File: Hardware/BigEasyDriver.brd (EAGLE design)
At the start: 36.8 x 30.5 mm, 53 parts, among them IC1 A4983ALT1, IC2 LM317L

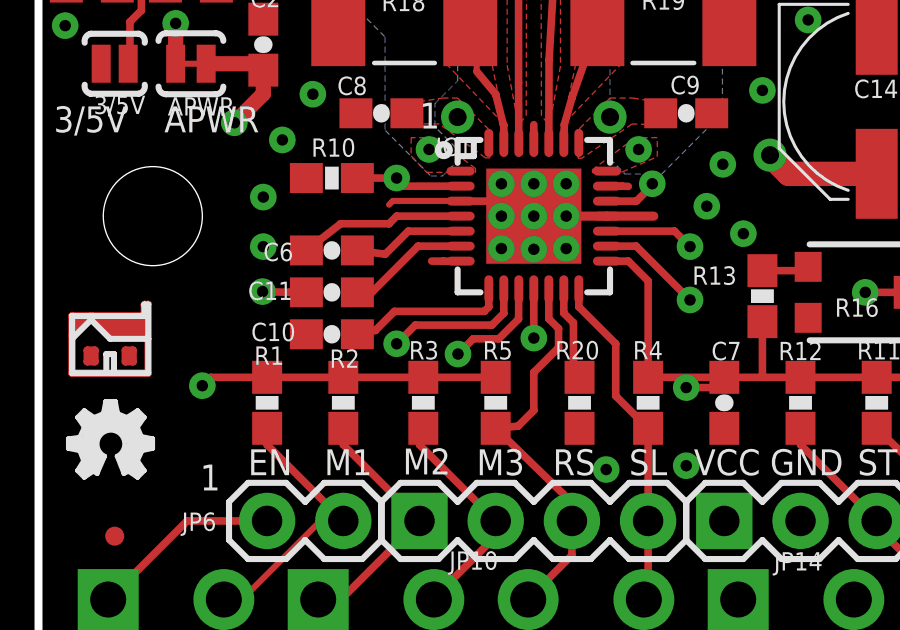
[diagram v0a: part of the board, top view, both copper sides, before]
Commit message: Changed Schematic Nets
Nets changed to new specifications
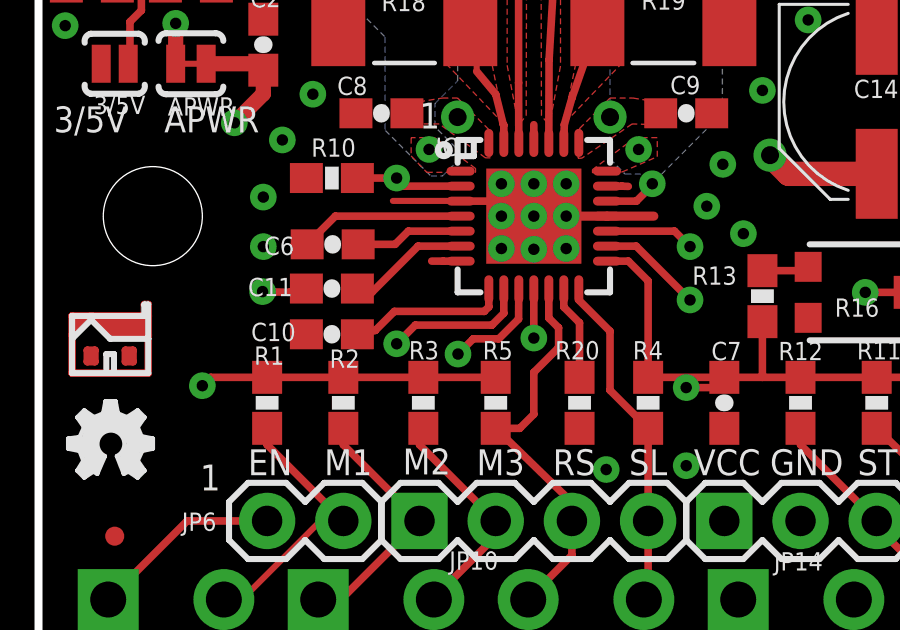
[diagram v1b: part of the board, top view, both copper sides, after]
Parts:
- moved C6 0.20 mm to (9.80, 14.3)
- moved C11 0.13 mm to (9.78, 12.8)
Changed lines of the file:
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@@
 <setting verticaltext="up"/>
 </settings>
-<grid distance="0.05" unitdist="inch" unit="inch" style="lines" multiple="1" display="yes" altdistance="0.005" altunitdist="inch" altunit="inch"/>
+<grid distance="0.05" unitdist="inch" unit="inch" style="lines" multiple="1" display="yes" altdistance="0.001" altunitdist="inch" altunit="inch"/>
 <layers>
 <layer number="1" name="Top" color="4" fill="1" visible="yes" active="yes"/>
@@
 <layer number="27" name="tValues" color="7" fill="1" visible="no" active="yes"/>
 <layer number="28" name="bValues" color="7" fill="1" visible="no" active="yes"/>
-<layer number="29" name="tStop" color="7" fill="3" visible="yes" active="yes"/>
+<layer number="29" name="tStop" color="7" fill="3" visible="no" active="yes"/>
 <layer number="30" name="bStop" color="7" fill="6" visible="no" active="yes"/>
 <layer number="31" name="tCream" color="7" fill="4" visible="no" active="yes"/>
@@
 <layer number="13" name="Route13" color="4" fill="5" visible="no" active="no"/>
 <layer number="14" name="Route14" color="1" fill="6" visible="no" active="no"/>
-<layer number="15" name="GND" color="13" fill="1" visible="yes" active="yes"/>
-<layer number="2" name="VCC" color="14" fill="1" visible="yes" active="yes"/>
+<layer number="15" name="GND" color="13" fill="1" visible="no" active="yes"/>
+<layer number="2" name="VCC" color="14" fill="1" visible="no" active="yes"/>
 <layer number="3" name="Route3" color="4" fill="3" visible="no" active="no"/>
 <layer number="4" name="Route4" color="1" fill="4" visible="no" active="no"/>
@@
 </class>
 </classes>
-<designrules name="SparkFun *">
+<designrules name="SparkFun">
 <description language="en">&lt;b&gt;EAGLE Design Rules&lt;/b&gt;
 &lt;p&gt;
@@
 <param name="mlMinCreamFrame" value="0mil"/>
 <param name="mlMaxCreamFrame" value="0mil"/>
-<param name="mlViaStopLimit" value="24mil"/>
+<param name="mlViaStopLimit" value="20mil"/>
 <param name="srRoundness" value="0"/>
 <param name="srMinRoundness" value="0mil"/>
@@
 <attribute name="VALUE" x="17.2466" y="6.8834" size="0.6096" layer="27"/>
 </element>
-<element name="C6" library="SparkFun" package="0603-CAP" value=".1uf" x="9.779" y="14.097" smashed="yes">
-<attribute name="NAME" x="7.493" y="13.7414" size="0.6096" layer="25" font="vector"/>
-<attribute name="VALUE" x="11.0236" y="13.8684" size="0.6096" layer="27" font="vector"/>
+<element name="C6" library="SparkFun" package="0603-CAP" value=".1uf" x="9.8044" y="14.3002" smashed="yes">
+<attribute name="NAME" x="7.5184" y="13.9446" size="0.6096" layer="25" font="vector"/>
+<attribute name="VALUE" x="11.049" y="14.0716" size="0.6096" layer="27" font="vector"/>
 </element>
 <element name="C7" library="SparkFun" package="0603-CAP" value=".1uf" x="22.86" y="9.017" smashed="yes" rot="R270">
@@
 <attribute name="VALUE" x="11.0236" y="11.0744" size="0.6096" layer="27" font="vector"/>
 </element>
-<element name="C11" library="SparkFun" package="0603-CAP" value=".1uf" x="9.779" y="12.7" smashed="yes" rot="R180">
-<attribute name="NAME" x="6.985" y="12.446" size="0.6096" layer="25" font="vector"/>
-<attribute name="VALUE" x="10.9728" y="12.446" size="0.6096" layer="27" font="vector"/>
+<element name="C11" library="SparkFun" package="0603-CAP" value=".1uf" x="9.779" y="12.827" smashed="yes" rot="R180">
+<attribute name="NAME" x="6.985" y="12.573" size="0.6096" layer="25" font="vector"/>
+<attribute name="VALUE" x="10.9728" y="12.573" size="0.6096" layer="27" font="vector"/>
 </element>
 <element name="D1" library="diode" package="DO-214AC" value="B340A-13-F" x="33.02" y="25.4" smashed="yes" rot="R90">
@@
 <wire x1="15.3035" y1="15.367" x2="15.4305" y2="15.24" width="0.254" layer="1"/>
 <wire x1="11.811" y1="15.748" x2="15.3035" y2="15.748" width="0.2032" layer="1"/>
-<wire x1="11.684" y1="15.621" x2="11.811" y2="15.748" width="0.2032" layer="1"/>
 <via x="15.4305" y="16.3195" extent="1-16" drill="0.381"/>
 <via x="16.51" y="16.3195" extent="1-16" drill="0.381"/>
@@
 <wire x1="9.271" y1="28.702" x2="8.763" y2="29.21" width="0.4064" layer="2"/>
 <wire x1="13.97" y1="18.542" x2="9.271" y2="23.241" width="0.4064" layer="2"/>
-<wire x1="8.929" y1="12.7" x2="8.3566" y2="12.7" width="0.254" layer="1"/>
+<wire x1="8.929" y1="12.827" x2="8.3566" y2="12.7" width="0.254" layer="1"/>
 <wire x1="8.3566" y1="12.7" x2="7.4676" y2="12.7254" width="0.254" layer="1"/>
 <wire x1="8.5344" y1="16.4084" x2="10.668" y2="18.542" width="0.254" layer="2"/>
@@
 <wire x1="16.3222" y1="2.4792" x2="17.78" y2="3.937" width="0.254" layer="1"/>
 <wire x1="17.78" y1="3.937" x2="17.78" y2="5.08" width="0.254" layer="1"/>
-<wire x1="17.01" y1="11.819" x2="17.01" y2="12.8" width="0.254" layer="1"/>
-<wire x1="17.3355" y1="11.4935" x2="17.01" y2="11.819" width="0.254" layer="1"/>
-<wire x1="17.3355" y1="10.8585" x2="17.3355" y2="11.4935" width="0.254" layer="1"/>
+<wire x1="17.01" y1="11.8444" x2="17.01" y2="12.8" width="0.254" layer="1"/>
+<wire x1="17.3355" y1="11.5189" x2="17.01" y2="11.8444" width="0.254" layer="1"/>
+<wire x1="17.3355" y1="10.8585" x2="17.3355" y2="11.5189" width="0.254" layer="1"/>
 <wire x1="16.51" y1="10.033" x2="17.3355" y2="10.8585" width="0.254" layer="1"/>
-<wire x1="16.51" y1="8.763" x2="16.51" y2="10.033" width="0.254" layer="1"/>
-<wire x1="15.987" y1="8.24" x2="16.51" y2="8.763" width="0.254" layer="1"/>
-<wire x1="15.24" y1="8.167" x2="15.987" y2="8.24" width="0.254" layer="1"/>
 <wire x1="17.78" y1="5.08" x2="17.78" y2="5.7" width="0.254" layer="1"/>
 <wire x1="17.78" y1="5.7" x2="15.24" y2="8.167" width="0.254" layer="1"/>
+<wire x1="16.51" y1="10.033" x2="16.51" y2="8.636" width="0.254" layer="1"/>
+<wire x1="16.51" y1="8.636" x2="16.041" y2="8.167" width="0.254" layer="1"/>
+<wire x1="16.041" y1="8.167" x2="15.24" y2="8.167" width="0.254" layer="1"/>
 </signal>
 <signal name="STEP">
@@
 <wire x1="20.1778" y1="2.46" x2="20.32" y2="2.6022" width="0.254" layer="1"/>
 <wire x1="20.32" y1="5.08" x2="20.32" y2="8.167" width="0.254" layer="1"/>
-<wire x1="18.01" y1="12.216" x2="18.01" y2="12.8001" width="0.254" layer="1"/>
-<wire x1="19.2405" y1="10.9855" x2="18.01" y2="12.216" width="0.254" layer="1"/>
-<wire x1="19.2405" y1="10.9855" x2="19.2405" y2="9.2465" width="0.254" layer="1"/>
-<wire x1="19.2405" y1="9.2465" x2="20.32" y2="8.167" width="0.254" layer="1"/>
+<wire x1="18.01" y1="12.8001" x2="18.01" y2="12.4446" width="0.254" layer="1"/>
+<wire x1="18.01" y1="12.4446" x2="19.05" y2="11.4046" width="0.254" layer="1"/>
+<wire x1="19.05" y1="11.4046" x2="19.05" y2="9.437" width="0.254" layer="1"/>
+<wire x1="19.05" y1="9.437" x2="20.32" y2="8.167" width="0.254" layer="1"/>
 </signal>
 <signal name="5V_ALT">
@@
 <contactref element="IC1" pad="P$4"/>
 <contactref element="C6" pad="1"/>
-<wire x1="11.938" y1="15.24" x2="14.0701" y2="15.24" width="0.254" layer="1"/>
-<wire x1="11.938" y1="15.24" x2="11.684" y2="14.986" width="0.254" layer="1"/>
-<wire x1="11.684" y1="14.986" x2="10.072" y2="14.986" width="0.254" layer="1"/>
-<wire x1="10.072" y1="14.986" x2="8.929" y2="14.097" width="0.254" layer="1"/>
+<wire x1="14.0701" y1="15.24" x2="9.8942" y2="15.24" width="0.254" layer="1"/>
+<wire x1="9.8942" y1="15.24" x2="8.9544" y2="14.3002" width="0.254" layer="1"/>
 </signal>
 <signal name="N$9">
@@
 <contactref element="C6" pad="2"/>
 <wire x1="12.327" y1="14.74" x2="14.0702" y2="14.74" width="0.254" layer="1"/>
-<wire x1="11.557" y1="13.97" x2="12.327" y2="14.74" width="0.254" layer="1"/>
-<wire x1="10.629" y1="14.097" x2="11.557" y2="13.97" width="0.254" layer="1"/>
+<wire x1="12.327" y1="14.74" x2="11.8872" y2="14.3002" width="0.254" layer="1"/>
+<wire x1="11.8872" y1="14.3002" x2="10.6544" y2="14.3002" width="0.254" layer="1"/>
 </signal>
 <signal name="N$19">
@@
 <contactref element="R20" pad="1"/>
 <wire x1="17.7546" y1="9.5654" x2="18.034" y2="9.867" width="0.254" layer="1"/>
-<wire x1="17.51" y1="12.0048" x2="17.51" y2="12.8001" width="0.254" layer="1"/>
-<wire x1="17.8308" y1="11.684" x2="17.51" y2="12.0048" width="0.254" layer="1"/>
-<wire x1="17.8308" y1="9.5908" x2="17.8308" y2="11.684" width="0.254" layer="1"/>
 <wire x1="18.034" y1="9.867" x2="17.8308" y2="9.5908" width="0.254" layer="1"/>
+<wire x1="18.1102" y1="9.9432" x2="18.034" y2="9.867" width="0.254" layer="1"/>
+<wire x1="17.51" y1="12.8001" x2="17.51" y2="12.208" width="0.254" layer="1"/>
+<wire x1="17.51" y1="12.208" x2="18.034" y2="11.684" width="0.254" layer="1"/>
+<wire x1="18.034" y1="11.684" x2="18.034" y2="9.867" width="0.254" layer="1"/>
 </signal>
 <signal name="N$20">
@@
 <wire x1="12.6525" y1="14.24" x2="14.0702" y2="14.24" width="0.254" layer="1"/>
 <wire x1="11.1125" y1="12.7" x2="12.6525" y2="14.24" width="0.254" layer="1"/>
-<wire x1="10.629" y1="12.7" x2="11.1125" y2="12.7" width="0.254" layer="1"/>
+<wire x1="10.629" y1="12.827" x2="11.1125" y2="12.7" width="0.254" layer="1"/>
 </signal>
 <signal name="MS3">

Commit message: Revert "Changed Schematic Nets"
This reverts commit ceb7b9bd87dc9e1a8942882cf4505f035ac33b39.
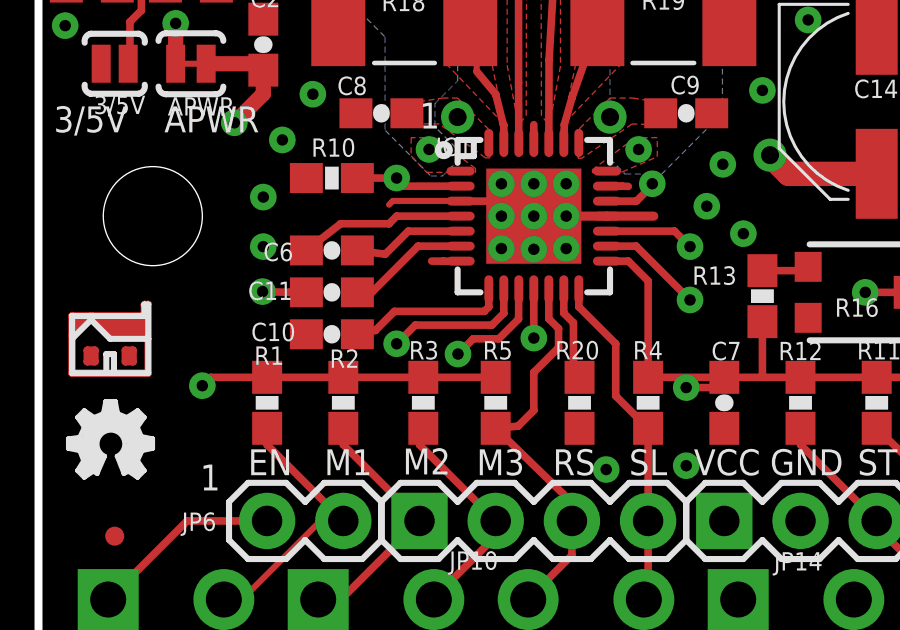
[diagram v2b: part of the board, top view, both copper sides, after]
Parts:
- moved C6 0.20 mm to (9.78, 14.1)
- moved C11 0.13 mm to (9.78, 12.7)
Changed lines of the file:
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@@
 <setting verticaltext="up"/>
 </settings>
-<grid distance="0.05" unitdist="inch" unit="inch" style="lines" multiple="1" display="yes" altdistance="0.001" altunitdist="inch" altunit="inch"/>
+<grid distance="0.05" unitdist="inch" unit="inch" style="lines" multiple="1" display="yes" altdistance="0.005" altunitdist="inch" altunit="inch"/>
 <layers>
 <layer number="1" name="Top" color="4" fill="1" visible="yes" active="yes"/>
@@
 <layer number="27" name="tValues" color="7" fill="1" visible="no" active="yes"/>
 <layer number="28" name="bValues" color="7" fill="1" visible="no" active="yes"/>
-<layer number="29" name="tStop" color="7" fill="3" visible="no" active="yes"/>
+<layer number="29" name="tStop" color="7" fill="3" visible="yes" active="yes"/>
 <layer number="30" name="bStop" color="7" fill="6" visible="no" active="yes"/>
 <layer number="31" name="tCream" color="7" fill="4" visible="no" active="yes"/>
@@
 <layer number="13" name="Route13" color="4" fill="5" visible="no" active="no"/>
 <layer number="14" name="Route14" color="1" fill="6" visible="no" active="no"/>
-<layer number="15" name="GND" color="13" fill="1" visible="no" active="yes"/>
-<layer number="2" name="VCC" color="14" fill="1" visible="no" active="yes"/>
+<layer number="15" name="GND" color="13" fill="1" visible="yes" active="yes"/>
+<layer number="2" name="VCC" color="14" fill="1" visible="yes" active="yes"/>
 <layer number="3" name="Route3" color="4" fill="3" visible="no" active="no"/>
 <layer number="4" name="Route4" color="1" fill="4" visible="no" active="no"/>
@@
 </class>
 </classes>
-<designrules name="SparkFun">
+<designrules name="SparkFun *">
 <description language="en">&lt;b&gt;EAGLE Design Rules&lt;/b&gt;
 &lt;p&gt;
@@
 <param name="mlMinCreamFrame" value="0mil"/>
 <param name="mlMaxCreamFrame" value="0mil"/>
-<param name="mlViaStopLimit" value="20mil"/>
+<param name="mlViaStopLimit" value="24mil"/>
 <param name="srRoundness" value="0"/>
 <param name="srMinRoundness" value="0mil"/>
@@
 <attribute name="VALUE" x="17.2466" y="6.8834" size="0.6096" layer="27"/>
 </element>
-<element name="C6" library="SparkFun" package="0603-CAP" value=".1uf" x="9.8044" y="14.3002" smashed="yes">
-<attribute name="NAME" x="7.5184" y="13.9446" size="0.6096" layer="25" font="vector"/>
-<attribute name="VALUE" x="11.049" y="14.0716" size="0.6096" layer="27" font="vector"/>
+<element name="C6" library="SparkFun" package="0603-CAP" value=".1uf" x="9.779" y="14.097" smashed="yes">
+<attribute name="NAME" x="7.493" y="13.7414" size="0.6096" layer="25" font="vector"/>
+<attribute name="VALUE" x="11.0236" y="13.8684" size="0.6096" layer="27" font="vector"/>
 </element>
 <element name="C7" library="SparkFun" package="0603-CAP" value=".1uf" x="22.86" y="9.017" smashed="yes" rot="R270">
@@
 <attribute name="VALUE" x="11.0236" y="11.0744" size="0.6096" layer="27" font="vector"/>
 </element>
-<element name="C11" library="SparkFun" package="0603-CAP" value=".1uf" x="9.779" y="12.827" smashed="yes" rot="R180">
-<attribute name="NAME" x="6.985" y="12.573" size="0.6096" layer="25" font="vector"/>
-<attribute name="VALUE" x="10.9728" y="12.573" size="0.6096" layer="27" font="vector"/>
+<element name="C11" library="SparkFun" package="0603-CAP" value=".1uf" x="9.779" y="12.7" smashed="yes" rot="R180">
+<attribute name="NAME" x="6.985" y="12.446" size="0.6096" layer="25" font="vector"/>
+<attribute name="VALUE" x="10.9728" y="12.446" size="0.6096" layer="27" font="vector"/>
 </element>
 <element name="D1" library="diode" package="DO-214AC" value="B340A-13-F" x="33.02" y="25.4" smashed="yes" rot="R90">
@@
 <wire x1="15.3035" y1="15.367" x2="15.4305" y2="15.24" width="0.254" layer="1"/>
 <wire x1="11.811" y1="15.748" x2="15.3035" y2="15.748" width="0.2032" layer="1"/>
+<wire x1="11.684" y1="15.621" x2="11.811" y2="15.748" width="0.2032" layer="1"/>
 <via x="15.4305" y="16.3195" extent="1-16" drill="0.381"/>
 <via x="16.51" y="16.3195" extent="1-16" drill="0.381"/>
@@
 <wire x1="9.271" y1="28.702" x2="8.763" y2="29.21" width="0.4064" layer="2"/>
 <wire x1="13.97" y1="18.542" x2="9.271" y2="23.241" width="0.4064" layer="2"/>
-<wire x1="8.929" y1="12.827" x2="8.3566" y2="12.7" width="0.254" layer="1"/>
+<wire x1="8.929" y1="12.7" x2="8.3566" y2="12.7" width="0.254" layer="1"/>
 <wire x1="8.3566" y1="12.7" x2="7.4676" y2="12.7254" width="0.254" layer="1"/>
 <wire x1="8.5344" y1="16.4084" x2="10.668" y2="18.542" width="0.254" layer="2"/>
@@
 <wire x1="16.3222" y1="2.4792" x2="17.78" y2="3.937" width="0.254" layer="1"/>
 <wire x1="17.78" y1="3.937" x2="17.78" y2="5.08" width="0.254" layer="1"/>
-<wire x1="17.01" y1="11.8444" x2="17.01" y2="12.8" width="0.254" layer="1"/>
-<wire x1="17.3355" y1="11.5189" x2="17.01" y2="11.8444" width="0.254" layer="1"/>
-<wire x1="17.3355" y1="10.8585" x2="17.3355" y2="11.5189" width="0.254" layer="1"/>
+<wire x1="17.01" y1="11.819" x2="17.01" y2="12.8" width="0.254" layer="1"/>
+<wire x1="17.3355" y1="11.4935" x2="17.01" y2="11.819" width="0.254" layer="1"/>
+<wire x1="17.3355" y1="10.8585" x2="17.3355" y2="11.4935" width="0.254" layer="1"/>
 <wire x1="16.51" y1="10.033" x2="17.3355" y2="10.8585" width="0.254" layer="1"/>
+<wire x1="16.51" y1="8.763" x2="16.51" y2="10.033" width="0.254" layer="1"/>
+<wire x1="15.987" y1="8.24" x2="16.51" y2="8.763" width="0.254" layer="1"/>
+<wire x1="15.24" y1="8.167" x2="15.987" y2="8.24" width="0.254" layer="1"/>
 <wire x1="17.78" y1="5.08" x2="17.78" y2="5.7" width="0.254" layer="1"/>
 <wire x1="17.78" y1="5.7" x2="15.24" y2="8.167" width="0.254" layer="1"/>
-<wire x1="16.51" y1="10.033" x2="16.51" y2="8.636" width="0.254" layer="1"/>
-<wire x1="16.51" y1="8.636" x2="16.041" y2="8.167" width="0.254" layer="1"/>
-<wire x1="16.041" y1="8.167" x2="15.24" y2="8.167" width="0.254" layer="1"/>
 </signal>
 <signal name="STEP">
@@
 <wire x1="20.1778" y1="2.46" x2="20.32" y2="2.6022" width="0.254" layer="1"/>
 <wire x1="20.32" y1="5.08" x2="20.32" y2="8.167" width="0.254" layer="1"/>
-<wire x1="18.01" y1="12.8001" x2="18.01" y2="12.4446" width="0.254" layer="1"/>
-<wire x1="18.01" y1="12.4446" x2="19.05" y2="11.4046" width="0.254" layer="1"/>
-<wire x1="19.05" y1="11.4046" x2="19.05" y2="9.437" width="0.254" layer="1"/>
-<wire x1="19.05" y1="9.437" x2="20.32" y2="8.167" width="0.254" layer="1"/>
+<wire x1="18.01" y1="12.216" x2="18.01" y2="12.8001" width="0.254" layer="1"/>
+<wire x1="19.2405" y1="10.9855" x2="18.01" y2="12.216" width="0.254" layer="1"/>
+<wire x1="19.2405" y1="10.9855" x2="19.2405" y2="9.2465" width="0.254" layer="1"/>
+<wire x1="19.2405" y1="9.2465" x2="20.32" y2="8.167" width="0.254" layer="1"/>
 </signal>
 <signal name="5V_ALT">
@@
 <contactref element="IC1" pad="P$4"/>
 <contactref element="C6" pad="1"/>
-<wire x1="14.0701" y1="15.24" x2="9.8942" y2="15.24" width="0.254" layer="1"/>
-<wire x1="9.8942" y1="15.24" x2="8.9544" y2="14.3002" width="0.254" layer="1"/>
+<wire x1="11.938" y1="15.24" x2="14.0701" y2="15.24" width="0.254" layer="1"/>
+<wire x1="11.938" y1="15.24" x2="11.684" y2="14.986" width="0.254" layer="1"/>
+<wire x1="11.684" y1="14.986" x2="10.072" y2="14.986" width="0.254" layer="1"/>
+<wire x1="10.072" y1="14.986" x2="8.929" y2="14.097" width="0.254" layer="1"/>
 </signal>
 <signal name="N$9">
@@
 <contactref element="C6" pad="2"/>
 <wire x1="12.327" y1="14.74" x2="14.0702" y2="14.74" width="0.254" layer="1"/>
-<wire x1="12.327" y1="14.74" x2="11.8872" y2="14.3002" width="0.254" layer="1"/>
-<wire x1="11.8872" y1="14.3002" x2="10.6544" y2="14.3002" width="0.254" layer="1"/>
+<wire x1="11.557" y1="13.97" x2="12.327" y2="14.74" width="0.254" layer="1"/>
+<wire x1="10.629" y1="14.097" x2="11.557" y2="13.97" width="0.254" layer="1"/>
 </signal>
 <signal name="N$19">
@@
 <contactref element="R20" pad="1"/>
 <wire x1="17.7546" y1="9.5654" x2="18.034" y2="9.867" width="0.254" layer="1"/>
+<wire x1="17.51" y1="12.0048" x2="17.51" y2="12.8001" width="0.254" layer="1"/>
+<wire x1="17.8308" y1="11.684" x2="17.51" y2="12.0048" width="0.254" layer="1"/>
+<wire x1="17.8308" y1="9.5908" x2="17.8308" y2="11.684" width="0.254" layer="1"/>
 <wire x1="18.034" y1="9.867" x2="17.8308" y2="9.5908" width="0.254" layer="1"/>
-<wire x1="18.1102" y1="9.9432" x2="18.034" y2="9.867" width="0.254" layer="1"/>
-<wire x1="17.51" y1="12.8001" x2="17.51" y2="12.208" width="0.254" layer="1"/>
-<wire x1="17.51" y1="12.208" x2="18.034" y2="11.684" width="0.254" layer="1"/>
-<wire x1="18.034" y1="11.684" x2="18.034" y2="9.867" width="0.254" layer="1"/>
 </signal>
 <signal name="N$20">
@@
 <wire x1="12.6525" y1="14.24" x2="14.0702" y2="14.24" width="0.254" layer="1"/>
 <wire x1="11.1125" y1="12.7" x2="12.6525" y2="14.24" width="0.254" layer="1"/>
-<wire x1="10.629" y1="12.827" x2="11.1125" y2="12.7" width="0.254" layer="1"/>
+<wire x1="10.629" y1="12.7" x2="11.1125" y2="12.7" width="0.254" layer="1"/>
 </signal>
 <signal name="MS3">
